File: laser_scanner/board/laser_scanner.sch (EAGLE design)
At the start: 8 parts

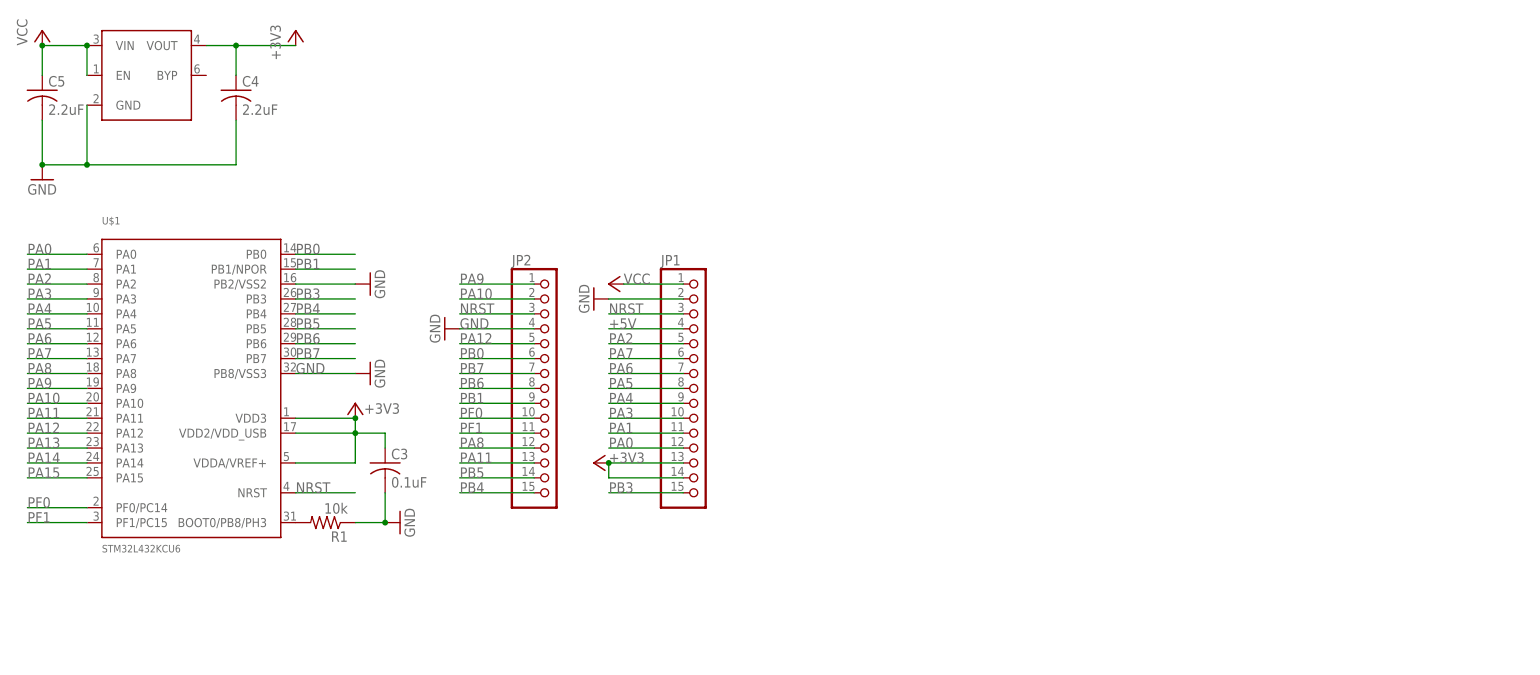
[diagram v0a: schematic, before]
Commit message: First pass at Othermilled laser scanner board. About to update for Bay Area Circuits order.
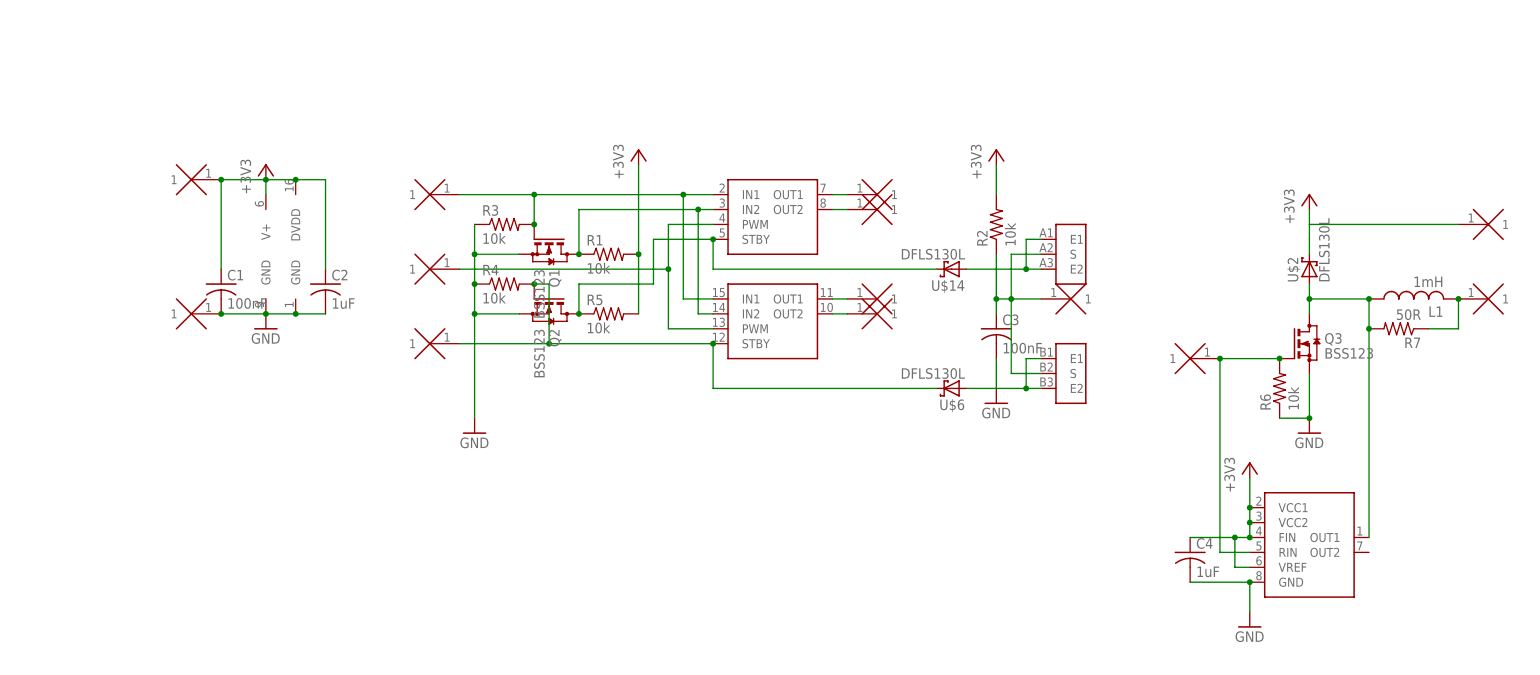
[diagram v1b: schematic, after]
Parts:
- removed C5: 2.2uF, rcl:C-USC0402
- removed JP1, JP2: (no value), pinhead:PINHD-1X15
- added C1: 100nF, rcl:C-USC0603
- added C2: 1uF, rcl:C-USC0603
- added GALVO_DIR, GALVO_PULSE, GALVO_SEL, GALVO_SENSE, GND, L+, L-, LASER_PWM, MA1, MA2, MB1, MB2, VCC: PAD-0.6_1.8, modular_robotics:PAD-0.6_1.8
- added L1: 1mH, modular_robotics:L-US
- added Q1, Q2, Q3: BSS123, transistor-small-signal:BSS123
- added R2, R3, R4, R5, R6: 10k, rcl:R-US_R0603
- added R7: 50R, rcl:R-US_R0603
- added U$14, U$2, U$6: DFLS130L, modular_robotics:DFLS130L
- added U$7: LASER_SLIDER, modular_robotics:LASER_SLIDER
- C3: value 0.1uF -> 100nF; device rcl:C-USC0402 -> rcl:C-USC0603
- C4: value 2.2uF -> 1uF; device rcl:C-USC0402 -> rcl:C-USC0603
- R1: device rcl:R-US_R0402 -> rcl:R-US_R0603
- U$1: value STM32L432KCU6 -> TB6552; device modular_robotics:STM32L432KCU6 -> modular_robotics:TB6552
- U$3: value MIC5305-MLF -> BD6211; device modular_robotics:MIC5305-MLF -> modular_robotics:BD6211
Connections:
- removed net +5V: JP1.4
- removed net NRST: JP1.3, JP2.3, U$1.NRST
- removed net PA0: JP1.12, U$1.PA0
- removed net PA1: JP1.11, U$1.PA1
- removed net PA10: JP2.2, U$1.PA10
- removed net PA11: JP2.13, U$1.PA11
- removed net PA12: JP2.5, U$1.PA12
- removed net PA13: U$1.PA13
- removed net PA14: U$1.PA14
- removed net PA15: U$1.PA15
- removed net PA2: JP1.5, U$1.PA2
- removed net PA3: JP1.10, U$1.PA3
- removed net PA4: JP1.9, U$1.PA4
- removed net PA5: JP1.8, U$1.PA5
- removed net PA6: JP1.7, U$1.PA6
- removed net PA7: JP1.6, U$1.PA7
- removed net PA8: JP2.12, U$1.PA8
- removed net PA9: JP2.1, U$1.PA9
- removed net PB0: JP2.6, U$1.PB0
- removed net PB1: JP2.9, U$1.PB1/NPOR
- removed net PB3: JP1.15, U$1.PB3
- removed net PB4: JP2.15, U$1.PB4
- removed net PB5: JP2.14, U$1.PB5
- removed net PB6: JP2.8, U$1.PB6
- removed net PB7: JP2.7, U$1.PB7
- removed net PF0: JP2.10, U$1.PF0/PC14
- removed net PF1: JP2.11, U$1.PF1/PC15
- removed net VCC: C5.1, JP1.1, U$3.EN, U$3.VIN
- new net N$10: LASER_PWM.1, Q3.G, R6.2, U$3.RIN
- new net N$11: U$14.A, U$7A.E1, U$7A.E2
- new net N$12: L1.1, Q3.D, R7.2, U$2.A, U$3.OUT1
- new net N$13: U$6.A, U$7B.E1, U$7B.E2
- new net N$14: C3.1, GALVO_SENSE.1, R2.1, U$7A.S, U$7B.S
- new net N$15: L-.1, L1.2, R7.1
- new net N$17: Q2.D, R5.1, U$14.C, U$1A.STBY
- new net N$2: MB2.1, U$1A.OUT2
- new net N$3: MA1.1, U$1B.OUT1
- new net N$4: MA2.1, U$1B.OUT2
- new net N$5: Q1.D, R1.1, U$1A.IN2, U$1B.IN2
- new net N$6: GALVO_SEL.1, Q2.G, R4.2, U$1B.STBY, U$6.C
- new net N$7: GALVO_DIR.1, Q1.G, R3.2, U$1A.IN1, U$1B.IN1
- new net N$9: GALVO_PULSE.1, U$1A.PWM, U$1B.PWM
- net +3V3: now also C1.1, C2.1, L+.1, R1.2, R2.2, R5.2, U$1DPWR.DVDD, U$1PWR.V+, U$2.C, U$3.FIN, U$3.VCC1, U$3.VCC2, U$3.VREF, VCC.1; no longer C3.1, JP1.13, JP1.14, U$1.VDD2/VDD_USB, U$1.VDD3, U$1.VDDA/VREF+, U$3.VOUT
- net GND: now also C1.2, C2.2, GND.1, Q1.S, Q2.S, Q3.S, R3.1, R4.1, R6.1, U$1DPWR.GND, U$1PWR.GND; no longer C5.2, JP1.2, JP2.4, R1.1, U$1.PB2/VSS2, U$1.PB8/VSS3
- net N$1: now also MB1.1, U$1A.OUT1; no longer R1.2, U$1.BOOT0/PB8/PH3
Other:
- moved on the sheet: C3, C4, R1

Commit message: Reworked laser scanner for BAC order
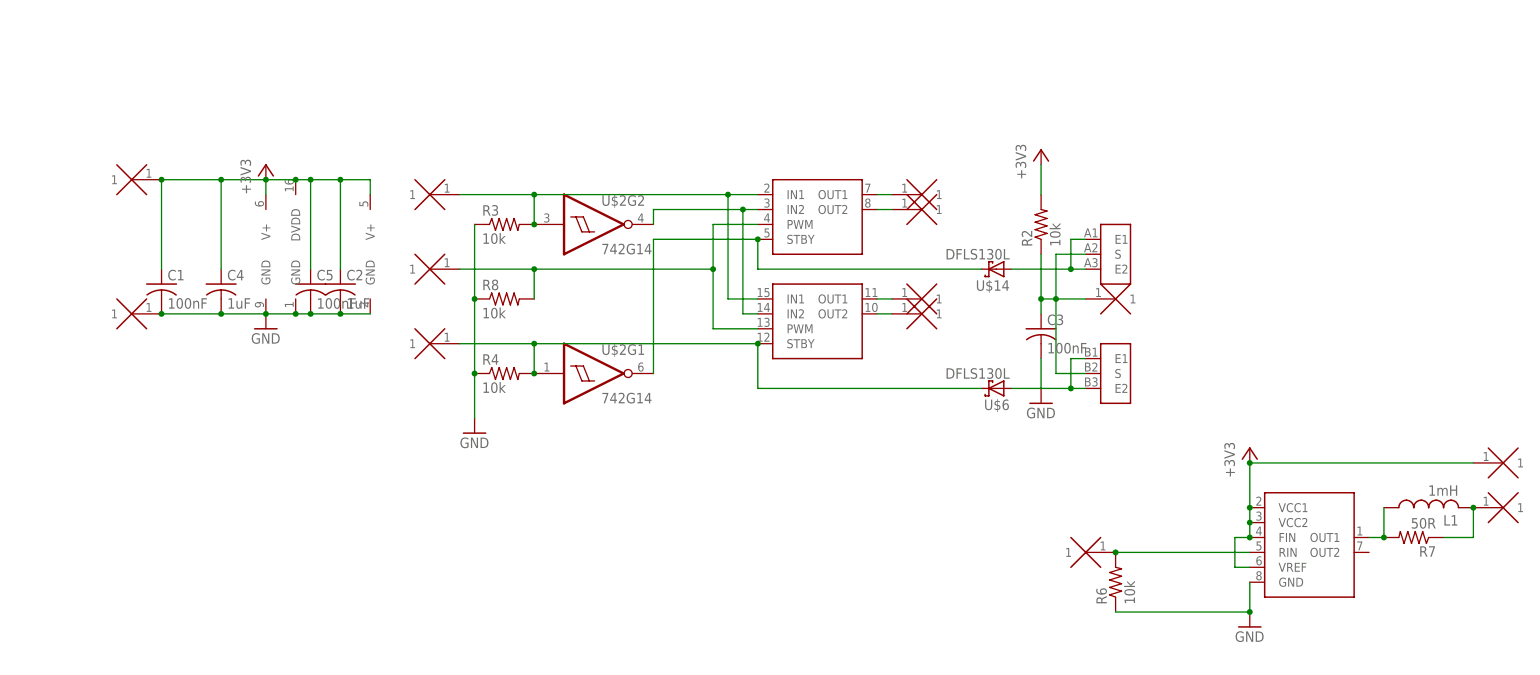
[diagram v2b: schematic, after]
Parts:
- removed Q1, Q2, Q3: BSS123, transistor-small-signal:BSS123
- removed R1, R5: 10k, rcl:R-US_R0603
- added C5: 100nF, rcl:C-USC0603
- added R8: 10k, rcl:R-US_R0603
- U$2: value DFLS130L -> 742G14; device modular_robotics:DFLS130L -> modular_robotics:742G14
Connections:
- net +3V3: now also C5.1, U$2PWR.V+; no longer R1.2, R5.2, U$2.C
- net GND: now also C5.2, R8.1, U$2PWR.GND; no longer Q1.S, Q2.S, Q3.S
- net N$10: no longer Q3.G
- net N$12: no longer Q3.D, U$2.A
- net N$17: now also U$2G1.O; no longer Q2.D, R5.1
- net N$5: now also U$2G2.O; no longer Q1.D, R1.1
- net N$6: now also U$2G1.I; no longer Q2.G
- net N$7: now also U$2G2.I; no longer Q1.G
- net N$9: now also R8.2
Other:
- moved on the sheet: C1, C2, C3, C4, L1, R2, R4, R6, R7, U$14, U$6

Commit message: Adding panelized laser scanner board.
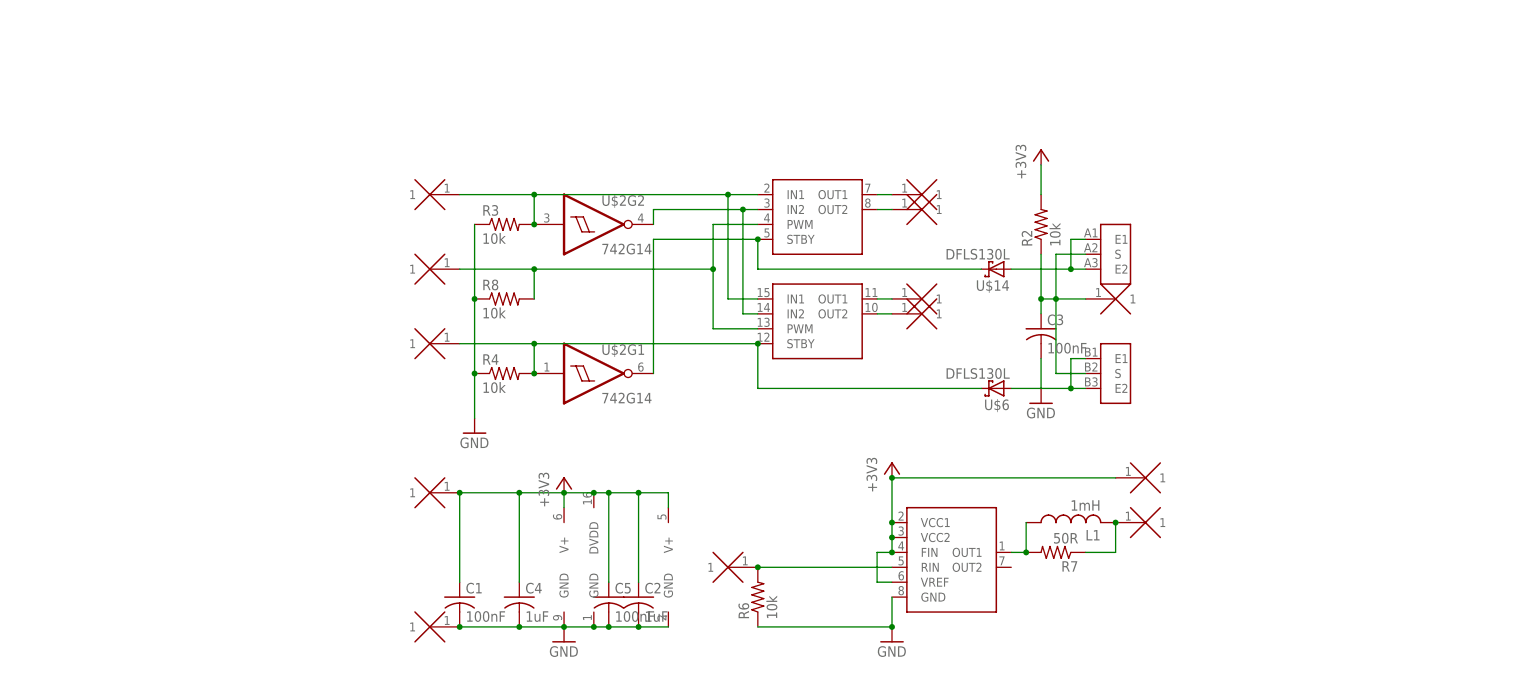
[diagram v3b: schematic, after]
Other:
- moved on the sheet: C1, C2, C4, C5, L1, R6, R7

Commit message: Added labels to wires. Fixed signal running through ground via.
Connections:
- net N$10 renamed LASER_PWM
- net N$14 renamed SENSE
- net N$6 renamed SEL
- net N$7 renamed DIR
- net N$9 renamed PULSE
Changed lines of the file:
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@@
 <instance part="GALVO_SEL" gate="G$1" x="55.88" y="33.02" rot="R180"/>
 <instance part="GALVO_PULSE" gate="G$1" x="55.88" y="45.72" rot="R180"/>
-<instance part="GALVO_SENSE" gate="G$1" x="172.72" y="40.64"/>
+<instance part="GALVO_SENSE" gate="G$1" x="180.34" y="40.64"/>
 <instance part="R3" gate="G$1" x="68.58" y="53.34"/>
 <instance part="GND2" gate="1" x="63.5" y="17.78"/>
@@
 </segment>
 </net>
-<net name="N$7" class="0">
+<net name="DIR" class="0">
 <segment>
 <pinref part="R3" gate="G$1" pin="2"/>
@@
 <pinref part="U$2" gate="G2" pin="I"/>
 <junction x="73.66" y="53.34"/>
-</segment>
-</net>
-<net name="N$6" class="0">
+<label x="60.96" y="58.42" size="1.778" layer="95"/>
+</segment>
+</net>
+<net name="SEL" class="0">
 <segment>
 <pinref part="U$6" gate="G$1" pin="C"/>
@@
 <junction x="73.66" y="33.02"/>
 <junction x="73.66" y="27.94"/>
-</segment>
-</net>
-<net name="N$9" class="0">
+<label x="73.66" y="33.02" size="1.778" layer="95"/>
+</segment>
+</net>
+<net name="PULSE" class="0">
 <segment>
 <pinref part="U$1" gate="A" pin="PWM"/>
@@
 <wire x1="73.66" y1="40.64" x2="73.66" y2="45.72" width="0.1524" layer="91"/>
 <junction x="73.66" y="45.72"/>
+<label x="78.74" y="43.18" size="1.778" layer="95"/>
 </segment>
 </net>
@@
 </segment>
 </net>
-<net name="N$14" class="0">
+<net name="SENSE" class="0">
 <segment>
 <pinref part="U$7" gate="A" pin="S"/>
@@
 <wire x1="162.56" y1="27.94" x2="167.64" y2="27.94" width="0.1524" layer="91"/>
 <pinref part="GALVO_SENSE" gate="G$1" pin="1"/>
-<wire x1="167.64" y1="40.64" x2="162.56" y2="40.64" width="0.1524" layer="91"/>
+<wire x1="175.26" y1="40.64" x2="162.56" y2="40.64" width="0.1524" layer="91"/>
 <junction x="162.56" y="40.64"/>
 <pinref part="C3" gate="G$1" pin="1"/>
@@
 <wire x1="162.56" y1="40.64" x2="160.02" y2="40.64" width="0.1524" layer="91"/>
 <junction x="160.02" y="40.64"/>
-</segment>
-</net>
-<net name="N$10" class="0">
+<label x="165.1" y="40.64" size="1.778" layer="95"/>
+</segment>
+</net>
+<net name="LASER_PWM" class="0">
 <segment>
 <pinref part="R6" gate="G$1" pin="2"/>
@@
 <pinref part="U$3" gate="G$1" pin="RIN"/>
 <wire x1="134.62" y1="-5.08" x2="111.76" y2="-5.08" width="0.1524" layer="91"/>
-</segment>
-</net>
+<label x="111.76" y="-5.08" size="1.778" layer="95"/>
+</segment>
+</net>
